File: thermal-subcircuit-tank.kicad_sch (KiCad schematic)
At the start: 16 parts, among them Q1 SQ3461EV, U2 TS5A3159-Q1, U3 TLV1805-Q1DBV

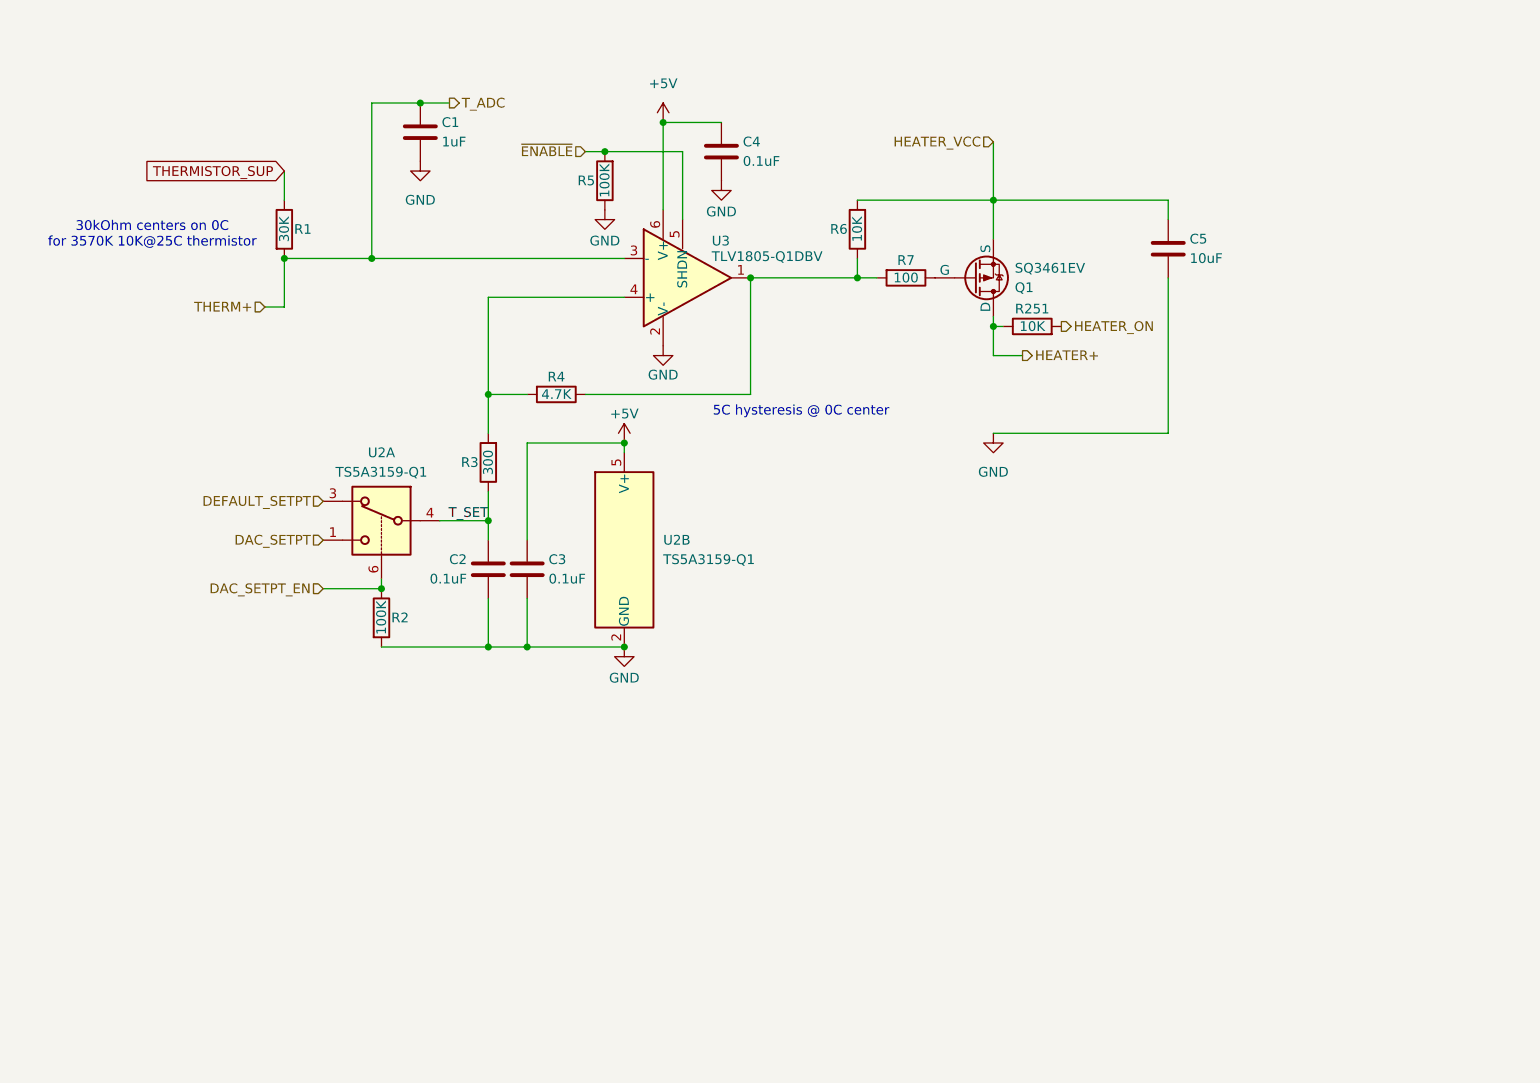
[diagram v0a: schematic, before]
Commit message: thermal circuit issue fixes
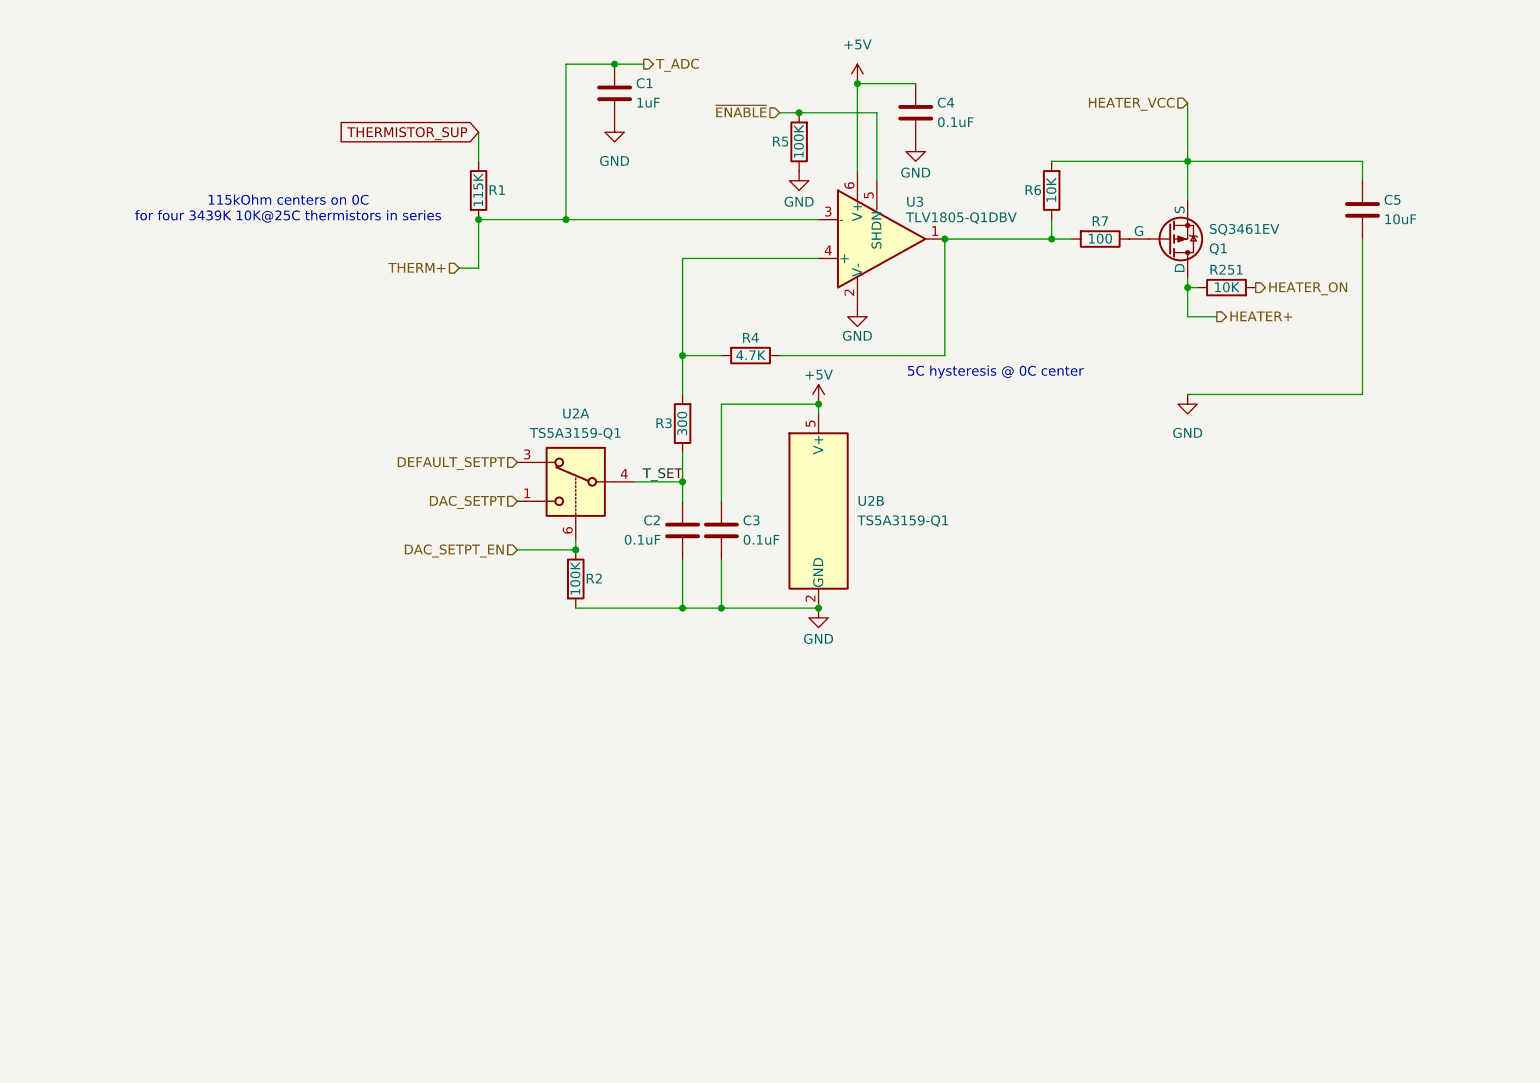
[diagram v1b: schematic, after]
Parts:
- R1: value 30K -> 115K
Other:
- note added: "115kOhm centers on 0C for four 3439K 10K@25C thermistors in series"
- note removed: "30kOhm centers on 0C for 3570K 10K@25C thermistor"
- moved on the sheet: C1, C2, C3, C4, C5, Q1, R1, R2, R251, R3, R4, R5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

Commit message: work
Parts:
- renumbered C1 to C71, C2 to C72, C3 to C73, C4 to C74, C5 to C75, Q1 to Q13, R251 to R100, R1 to R93, R2 to R94, R3 to R95, R4 to R96, R5 to R97, R6 to R98, R7 to R99, U2 to U26, U3 to U27

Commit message: work
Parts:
- removed C71: 1uF, symbol Device:C
- removed C72, C73, C74: 0.1uF, symbol Device:C
- removed C75: 10uF, symbol Device:C
- removed R100, R98: 10K, symbol Device:R
- removed R93: 115K, symbol Device:R
- removed R94, R97: 100K, symbol Device:R
- removed R95: 300, symbol Device:R
- removed R96: 4.7K, symbol Device:R
- removed R99: 100, symbol Device:R
- removed U26: TS5A3159-Q1, Package_TO_SOT_SMD:SOT-23-6, symbol Analog_Switch:TS5A3159ADBVR
- removed U27: TLV1805-Q1DBV, Package_TO_SOT_SMD:SOT-23-6, symbol femta-control-custom:TLV1805-Q1DBV
- added C61: 1uF, symbol Device:C
- added C62, C63, C64: 0.1uF, symbol Device:C
- added C65: 10uF, symbol Device:C
- added R111: 115K, symbol Device:R
- added R112, R115: 100K, symbol Device:R
- added R113: 300, symbol Device:R
- added R114: 4.7K, symbol Device:R
- added R116, R118: 10K, symbol Device:R
- added R117: 100, symbol Device:R
- added U25: TS5A3159-Q1, Package_TO_SOT_SMD:SOT-23-6, symbol Analog_Switch:TS5A3159ADBVR
- added U26: TLV1805-Q1DBV, Package_TO_SOT_SMD:SOT-23-6, symbol femta-control-custom:TLV1805-Q1DBV
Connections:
- net +5V: now also C63.1, C64.1, U25.5 (V+), U26.6 (V+)
- net DAC_SETPT: now also U25.1
- net DAC_SETPT_EN: now also R112.1, U25.6
- net DEFAULT_SETPT: now also U25.3
- net GND: now also C61.2, C62.2, C63.2, C64.2, C65.2, R112.2, R115.1, U25.2 (GND), U26.2 (V-)
- net HEATER+: now also R118.1
- net HEATER_ON: now also R118.2
- net HEATER_VCC: now also C65.1, R116.2
- net THERM+: now also C61.1, R111.2, U26.3 (-)
- net THERMISTOR_SUP: now also R111.1
- net T_SET: now also C62.1, R113.1, U25.4
- net ~{ENABLE}: now also R115.2, U26.5 (SHDN)
- net at Q13.3 (G): now also R117.1
- new net: R114.1, R116.1, R117.2, U26.1
- new net: R113.2, R114.2, U26.4 (+)

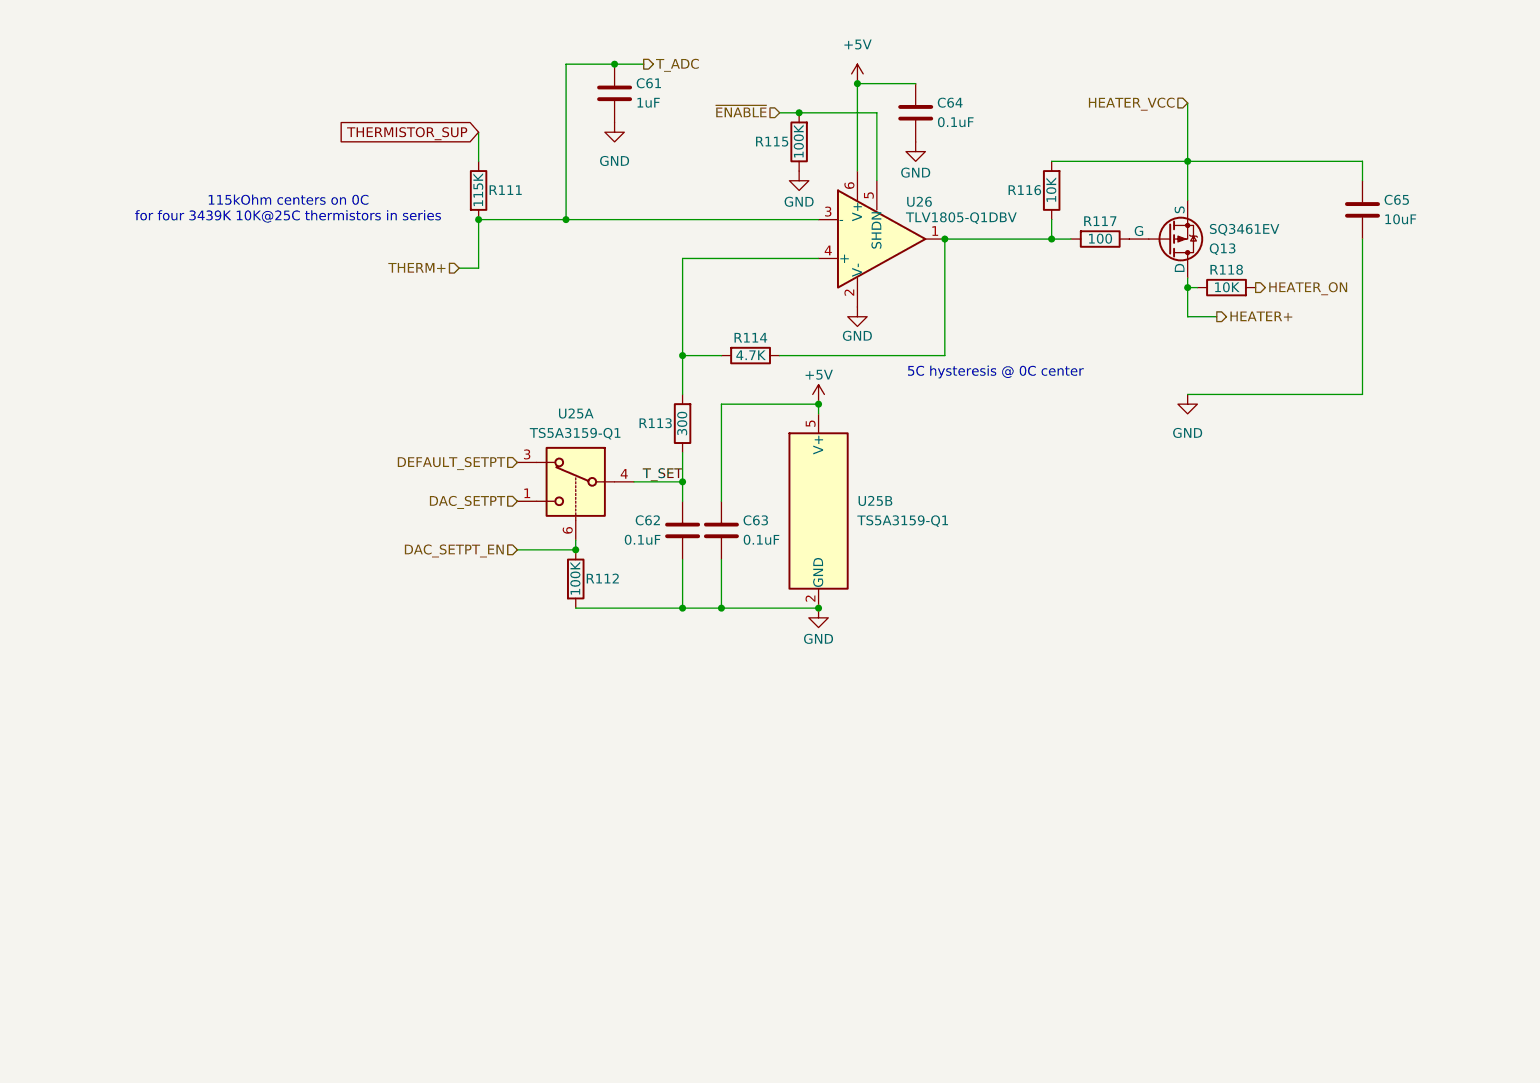
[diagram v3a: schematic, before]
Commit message: consolidate heaters
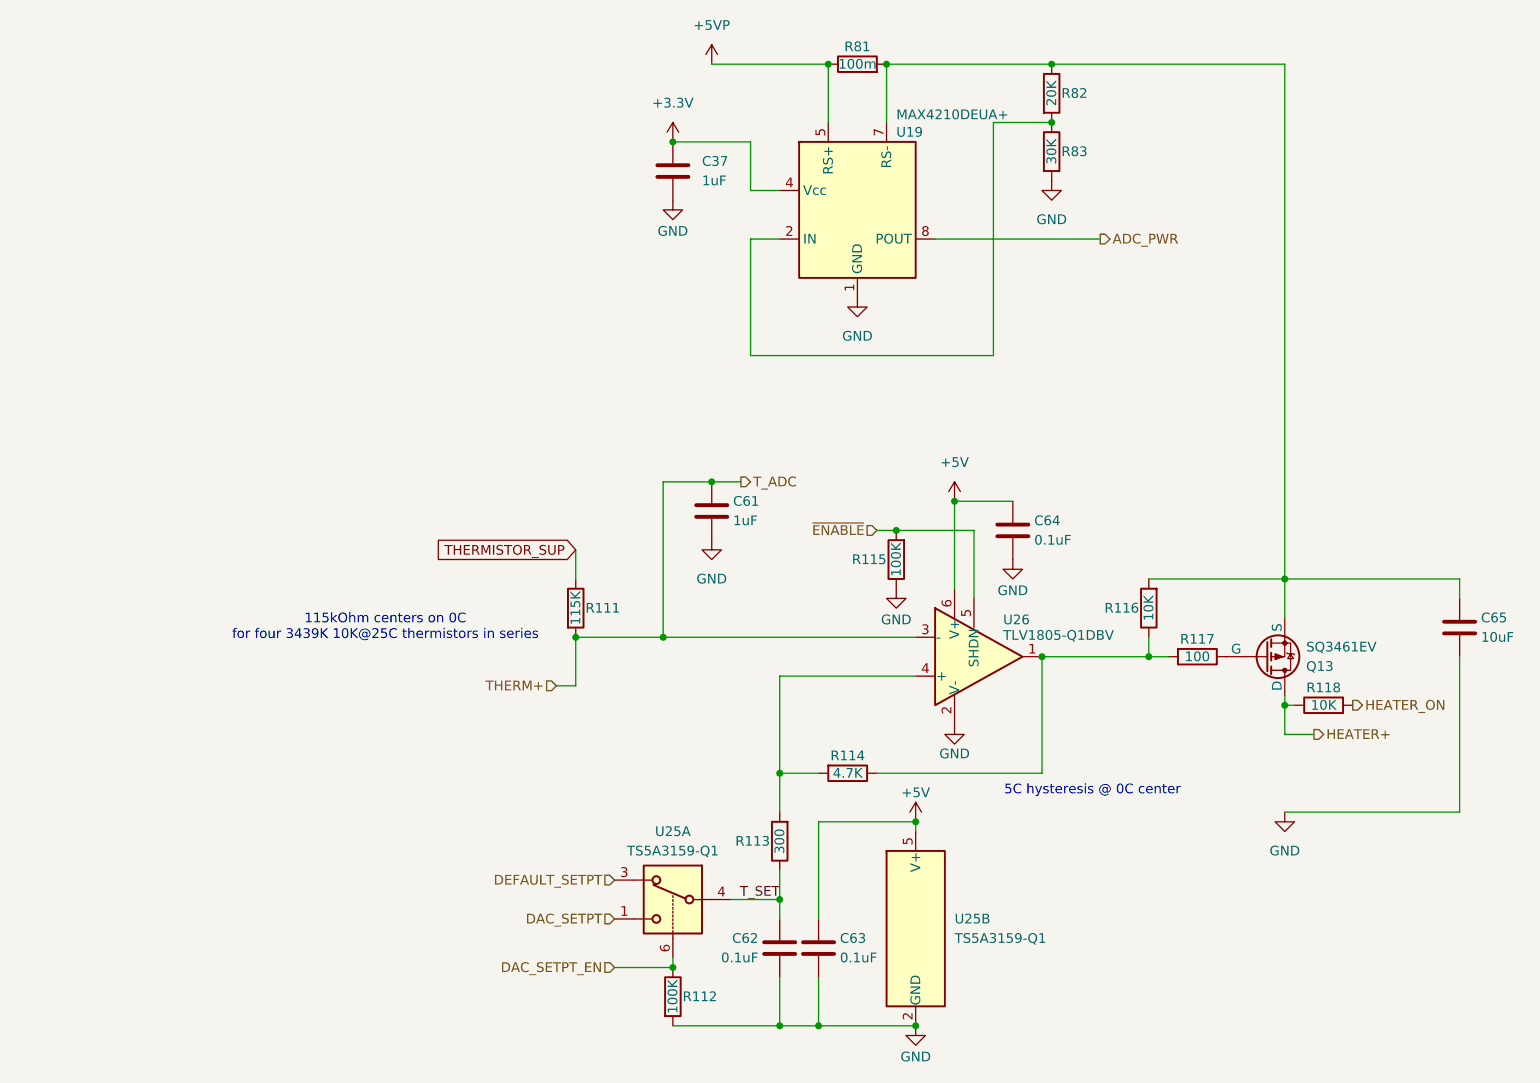
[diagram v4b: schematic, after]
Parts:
- added C37: 1uF, symbol Device:C
- added R81: 100m, symbol Device:R
- added R82: 20K, symbol Device:R
- added R83: 30K, symbol Device:R
- added U19: MAX4210DEUA+, symbol femta-control-custom:MAX4210
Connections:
- net GND: now also C37.2, R83.2, U19.1 (GND)
- net HEATER_VCC: no longer names the net of C65.1, Q13.4 (S), R116.2
- net HEATER_VCC: now also R81.2, R82.1, U19.7 (RS-)
- new net: R82.2, R83.1, U19.2 (IN)
- new net: U19.3 (NC), U19.6 (NC)
- new net +3.3V: C37.1, U19.4 (Vcc)
- new net +5VP: R81.1, U19.5 (RS+)
- new net ADC_PWR: U19.8 (POUT)
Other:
- moved on the sheet: C61, C62, C63, C64, C65, Q13, R111, R112, R113, R114, R115, R116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

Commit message: work
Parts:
- added J11, J12, J13, J14: THERMISTOR, symbol Connector:Conn_01x02_Socket
- added J15, J16: HEATER, symbol Connector:Conn_01x02_Socket
- added R101: 30K, symbol Device:R
- R118: value 10K -> 20K
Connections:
- net GND: now also J14.1 (Pin_1), J15.1 (Pin_1), J16.1 (Pin_1), R101.2
- net HEATER_ON: now also R101.1
- net HEATER+: no longer names the net of Q13.1 (D), Q13.2 (D), Q13.5 (D), Q13.6 (D), R118.1
- net HEATER+: now also J15.2 (Pin_2), J16.2 (Pin_2)
- net THERM+ renamed T_ADC
- net T_ADC: now also J11.2 (Pin_2)
- new net: J11.1 (Pin_1), J12.2 (Pin_2)
- new net: J12.1 (Pin_1), J13.2 (Pin_2)
- new net: J13.1 (Pin_1), J14.2 (Pin_2)
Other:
- moved on the sheet: R118

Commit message: lots and lots and lots of work
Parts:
- R81: value 100m -> 50m
- R82: value 20K -> 51K
- R83: value 30K -> 13K
- U19: value MAX4210DEUA+ -> MAX4210FEUA+
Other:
- note added: "V(pout) = 0.416*POUT, 7.933W max power"
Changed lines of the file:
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@@
+		)
+	)
+	(text "V(pout) = 0.416*POUT, 7.933W max power"
+		(exclude_from_sim no)
+		(at 128.778 85.852 0)
+		(effects
+			(font
+				(size 1.27 1.27)
+			)
 		)
 	)
@@
 			)
 		)
-		(property "Value" "MAX4210DEUA+"
+		(property "Value" "MAX4210FEUA+"
 			(at 133.35 51.054 0)
 			(do_not_autoplace yes)
@@
 			)
 		)
-		(property "Value" "100m"
+		(property "Value" "50m"
 			(at 128.27 44.45 90)
 			(effects
@@
 			)
 		)
-		(property "Value" "30K"
+		(property "Value" "13K"
 			(at 153.67 55.88 90)
 			(effects
@@
 			)
 		)
-		(property "Value" "20K"
+		(property "Value" "51K"
 			(at 153.67 48.26 90)
 			(effects

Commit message: 540 COMPONENTS I AM LOSING MY MINDDDDDD
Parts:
- renumbered C37 to C114, C61 to C115, C62 to C116, C63 to C117, C64 to C118, C65 to C119, J11 to J19, J12 to J20, J13 to J21, J14 to J22, J15 to J23, J16 to J24, Q13 to Q25, R111 to R186, R112 to R187, R113 to R188, R114 to R189, R81 to R190, R115 to R191, R82 to R192, R83 to R193, R116 to R194, R117 to R195, R118 to R196, R101 to R197, U25 to U94, U19 to U95, U26 to U96
